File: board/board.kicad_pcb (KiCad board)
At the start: 2 copper layers, 37 x 29 mm, 25 parts, among them J1 013_PoE_rectified, J2 003_power, U1 MP8007, U2 POE13P-50L

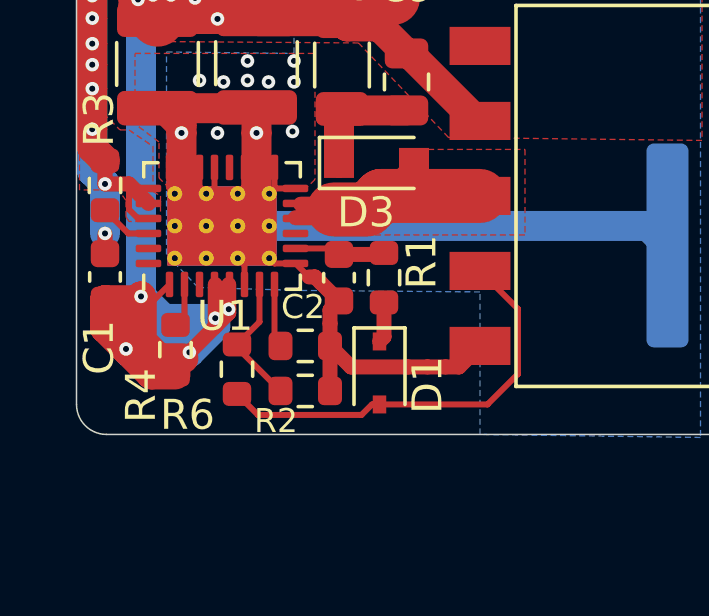
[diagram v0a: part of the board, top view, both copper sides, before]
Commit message: updated voltage and current setting resistors
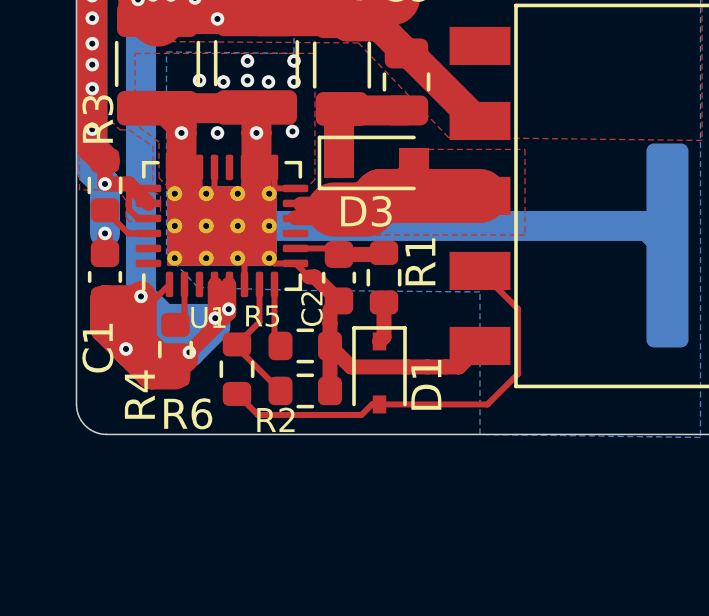
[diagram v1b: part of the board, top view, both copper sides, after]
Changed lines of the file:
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@@
     (property "Sheetname" "flyback")
     (attr smd)
-    (fp_text reference "C2" (at 0.975 1.2 180) (layer "F.SilkS")
-      (effects (font (size 0.8 0.8) (thickness 0.15)))
+    (fp_text reference "C2" (at 1.025 0.875 -90) (layer "F.SilkS")
+      (effects (font (size 0.7 0.7) (thickness 0.15)))
     )
     (fp_text value "1uF" (at 0 1.43 90) (layer "F.Fab")
@@
     (property "Sheetname" "flyback")
     (attr smd)
-    (fp_text reference "R5" (at -0.175 -1.65) (layer "B.SilkS")
-      (effects (font (size 1 1) (thickness 0.15)) (justify mirror))
+    (fp_text reference "R5" (at -1.425 -0.975) (layer "F.SilkS")
+      (effects (font (size 0.7 0.7) (thickness 0.15)))
     )
     (fp_text value "49.9k" (at 0.225 1.7) (layer "B.Fab")
@@
     (property "Sheetname" "flyback")
     (attr smd)
-    (fp_text reference "U1" (at -3 0.1) (layer "F.SilkS")
-      (effects (font (size 1 1) (thickness 0.15)))
+    (fp_text reference "U1" (at -3.075 -0.45) (layer "F.SilkS")
+      (effects (font (size 0.7 0.7) (thickness 0.15)))
     )
     (fp_text value "MP8007" (at 0 3.82 90) (layer "F.Fab")
